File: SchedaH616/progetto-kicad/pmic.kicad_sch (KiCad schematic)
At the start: 96 parts, among them U201 RK809-5, U202 TCS4525_WT, U203 TPS563201DDCR, U204 AP2112K-1.8TRG1, U205 AP2112K-2.5TRG1, Y201 32.768kHz

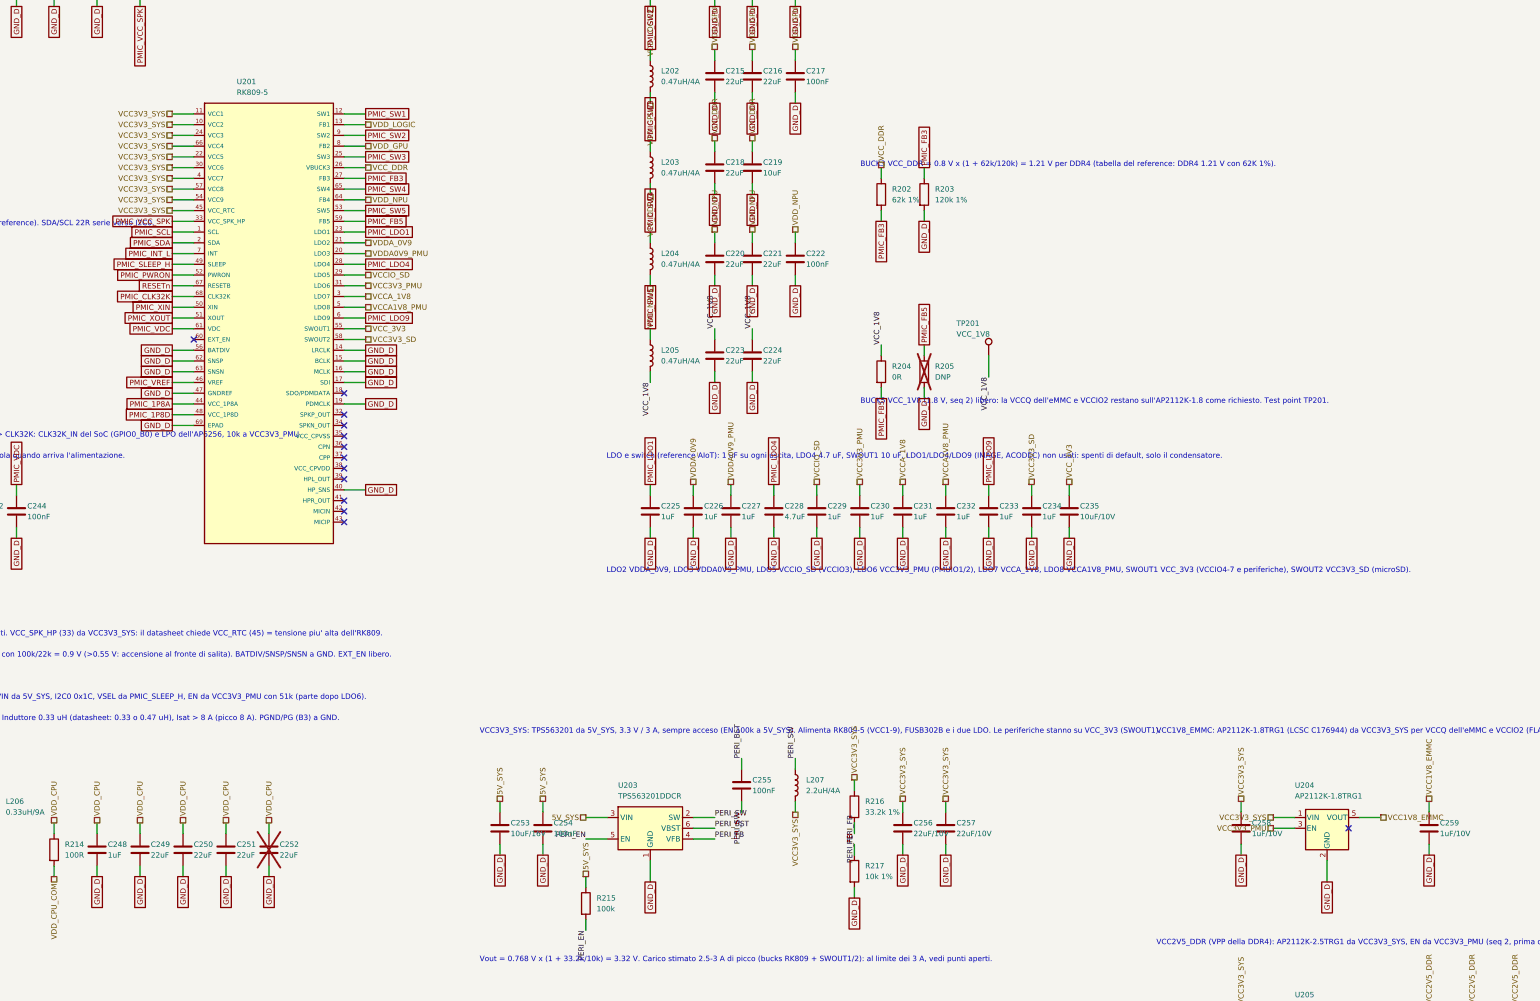
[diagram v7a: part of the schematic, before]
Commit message: SchedaH616: componenti specifici dalla libreria MIKILAB
- simbolo e footprint MIKILAB per RK809-5, TCS4525, K4AAG165WA-BCWE, FEMDNN064G-C9A61,
  AP2112K-1.8TRG1, TPS56637RPAR, TPS2121RUXR, SY6280AAC, TPS563201DDCR, TPS2553DBVR,
  TYPE-C-31-M-12, FH12-30S-0.5SH, FPC-05F-28PH20, HR911130C, 25AA02E48T-I/OT, DM3AT-SF-PEJM5;
  simbolo MIKILAB per l'AP6256
- restano nella libreria di progetto: RK3568 (pad EasyEDA da 0.35 mm, niente fanout 5/5 mil),
  simbolo RTL8211F (quello MIKILAB ha pin di alimentazione nascosti), footprint AP6256 LGA-47,
  portapila BS-12; motivazioni in docs/scelte-progetto.md
- kilib.mik() carica simboli e footprint dalla libreria (variabile MIKILAB); matrice ERC:
  pin unspecified dei simboli EasyEDA OK
- netlist identica a 4ca35fc (439 componenti, 314 net); ERC 0, parita' 0, DRC 0 (solo
  collegamenti da fare); footprint corretti nella libreria MIKILAB 8b990c4

Co-Authored-By: Claude Opus 5.5 (1M context) <noreply@anthropic.com>
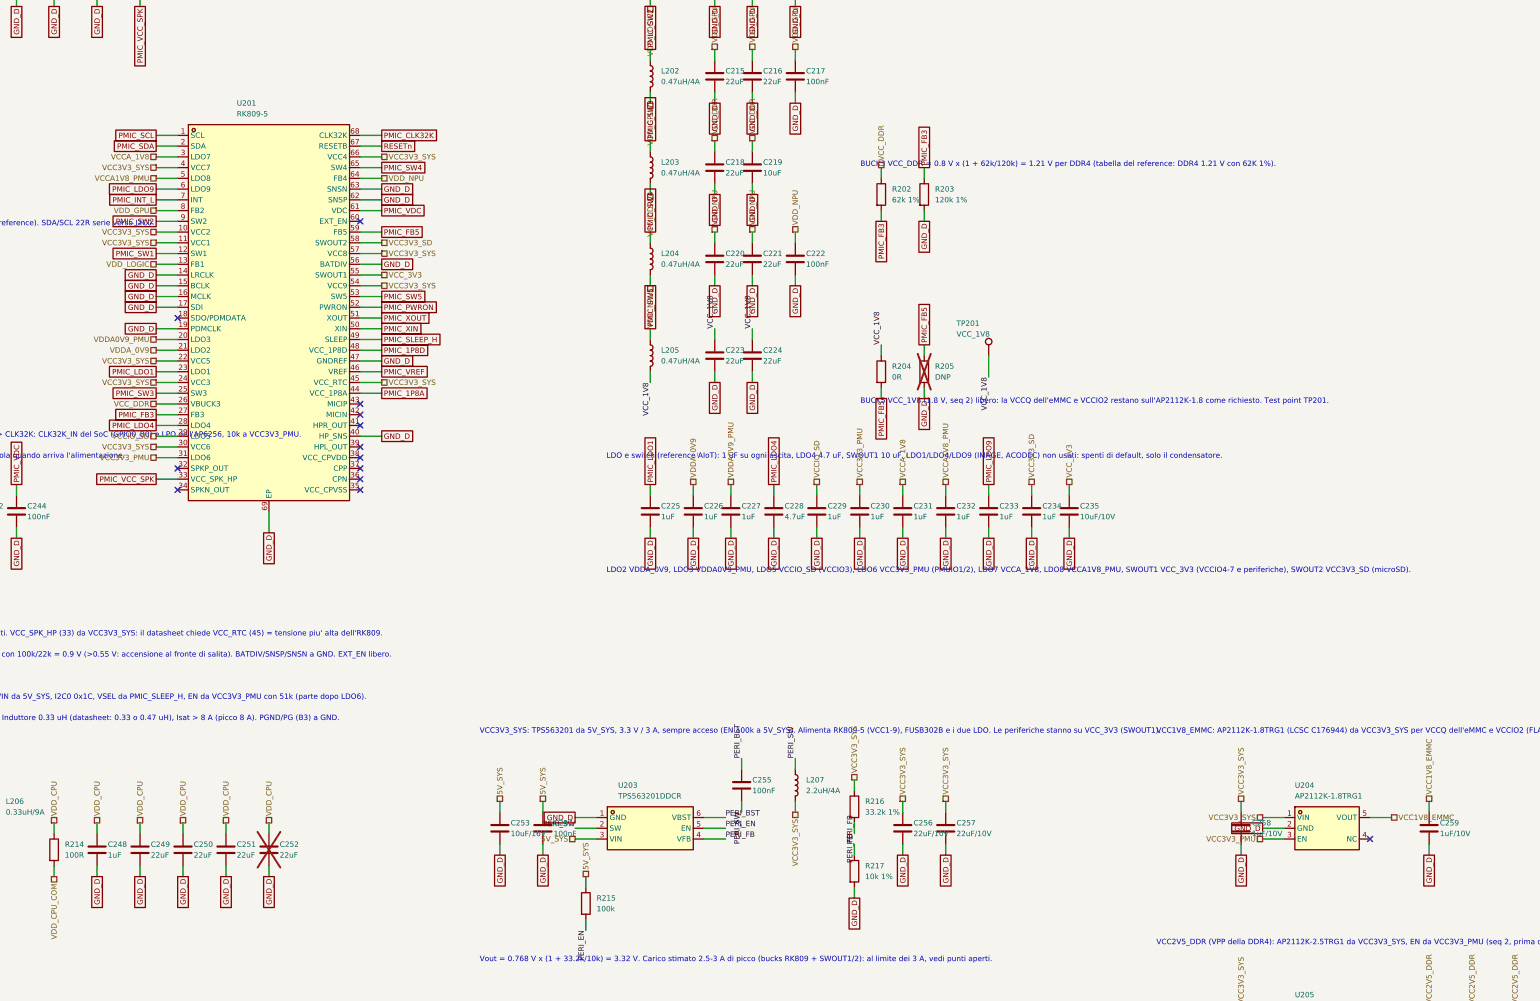
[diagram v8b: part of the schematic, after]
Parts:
- removed U201: RK809-5, Package_DFN_QFN:ArtInChip_QFN-68-1EP_7x7mm_P0.35mm_EP5.49x5.49mm, symbol Scheda:RK809-5
- removed U202: TCS4525_WT, Package_CSP:DiodesInc_GEA20_WLCSP-20_1.7x2.1mm_Layout4x5_P0.4mm, symbol Scheda:TCS4525
- removed U203: TPS563201DDCR, Package_TO_SOT_SMD:SOT-23-6, symbol Regulator_Switching:TPS563201
- removed U204: AP2112K-1.8TRG1, Package_TO_SOT_SMD:SOT-23-5, symbol Regulator_Linear:AP2112K-1.8
- added U201: RK809-5, MIKILAB_RK809_5:QFN-68_L7.0-W7.0-P0.35-BL-EP5.5, symbol MIKILAB_RK809_5:RK809-5
- added U202: TCS4525_WT, MIKILAB_TCS4525:TCS4525_WLCSP-20_1.6x2.0mm_P0.4mm, symbol MIKILAB_TCS4525:TCS4525
- added U203: TPS563201DDCR, MIKILAB_TPS563201DDCR:TPS563201DDCR_SOT-23-6_L2.9-W1.6-P0.95-LS2.8-BR, symbol MIKILAB_TPS563201DDCR:TPS563201DDCR
- added U204: AP2112K-1.8TRG1, MIKILAB_AP2112K_1_8TRG1:SOT-25_L3.0-W1.6-P0.95-LS2.8-BL, symbol MIKILAB_AP2112K_1_8TRG1:AP2112K-1.8TRG1
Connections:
- net 5V_SYS: now also U202.D1 (AVIN), U202.D2 (PVIN), U202.E1 (PVIN), U202.E2 (PVIN), U203.3 (VIN)
- net GND_D: now also U201.14 (LRCLK), U201.15 (BCLK), U201.16 (MCLK), U201.17 (SDI), U201.19 (PDMCLK), U201.40 (HP_SNS), U201.47 (GNDREF), U201.56 (BATDIV), U201.62 (SNSP), U201.63 (SNSN), U201.69 (EP), U202.B2 (PGND), U202.B3 (PGND/PG), U202.B4 (AGND), U202.C1 (PGND), U202.C2 (PGND), U202.C3 (PGND), U202.C4 (PGND), U203.1 (GND), U204.2 (GND)
- net I2C0_SCL: now also U202.A3 (SCL)
- net I2C0_SDA: now also U202.B1 (SDA)
- net PERI_BST: now also U203.6 (VBST)
- net PERI_EN: now also U203.5 (EN)
- net PERI_FB: now also U203.4 (VFB)
- net PERI_SW: now also U203.2 (SW)
- net PMIC_1P8A: now also U201.44 (VCC_1P8A)
- net PMIC_1P8D: now also U201.48 (VCC_1P8D)
- net PMIC_CLK32K: now also U201.68 (CLK32K)
- net PMIC_FB3: now also U201.27 (FB3)
- net PMIC_FB5: now also U201.59 (FB5)
- net PMIC_INT_L: now also U201.7 (INT)
- net PMIC_LDO1: now also U201.23 (LDO1)
- net PMIC_LDO4: now also U201.28 (LDO4)
- net PMIC_LDO9: now also U201.6 (LDO9)
- net PMIC_PWRON: now also U201.52 (PWRON)
- net PMIC_SCL: now also U201.1 (SCL)
- net PMIC_SDA: now also U201.2 (SDA)
- net PMIC_SLEEP_H: now also U201.49 (SLEEP), U202.A1 (VSEL)
- net PMIC_SW1: now also U201.12 (SW1)
- net PMIC_SW2: now also U201.9 (SW2)
- net PMIC_SW3: now also U201.25 (SW3)
- net PMIC_SW4: now also U201.65 (SW4)
- net PMIC_SW5: now also U201.53 (SW5)
- net PMIC_VCC_SPK: now also U201.33 (VCC_SPK_HP)
- net PMIC_VDC: now also U201.61 (VDC)
- net PMIC_VREF: now also U201.46 (VREF)
- net PMIC_XIN: now also U201.50 (XIN)
- net PMIC_XOUT: now also U201.51 (XOUT)
- net RESETn: now also U201.67 (RESETB)
- net TCS_EN: now also U202.A2 (EN)
- net TCS_SW: now also U202.D3 (SW), U202.D4 (SW), U202.E3 (SW), U202.E4 (SW)
- net VCC1V8_EMMC: now also U204.5 (VOUT)
- net VCC3V3_PMU: now also U201.31 (LDO6), U204.3 (EN)
- net VCC3V3_SD: now also U201.58 (SWOUT2)
- net VCC3V3_SYS: now also U201.10 (VCC2), U201.11 (VCC1), U201.22 (VCC5), U201.24 (VCC3), U201.30 (VCC6), U201.4 (VCC7), U201.45 (VCC_RTC), U201.54 (VCC9), U201.57 (VCC8), U201.66 (VCC4), U204.1 (VIN)
- net VCCA1V8_PMU: now also U201.5 (LDO8)
- net VCCA_1V8: now also U201.3 (LDO7)
- net VCCIO_SD: now also U201.29 (LDO5)
- net VCC_3V3: now also U201.55 (SWOUT1)
- net VCC_DDR: now also U201.26 (VBUCK3)
- net VDDA0V9_PMU: now also U201.20 (LDO3)
- net VDDA_0V9: now also U201.21 (LDO2)
- net VDD_CPU_COM: now also U202.A4 (FB)
- net VDD_GPU: now also U201.8 (FB2)
- net VDD_LOGIC: now also U201.13 (FB1)
- net VDD_NPU: now also U201.64 (FB4)
